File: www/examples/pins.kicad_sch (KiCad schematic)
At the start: 11 parts, among them U101 ATSAMD09C13A-SS, U102 ATSAMD09C13A-SS, U103 ATSAMD09C13A-SS, U104 ATSAMD09C13A-SS, U105 ATSAMD09C13A-SS, U106 ATSAMD09C13A-SS, U107 ATSAMD09C13A-SS, U108 ATSAMD09C13A-SS, U109 ATSAMD09C13A-SS, U110 ATSAMD09C13A-SS, U111 ATSAMD09C13A-SS

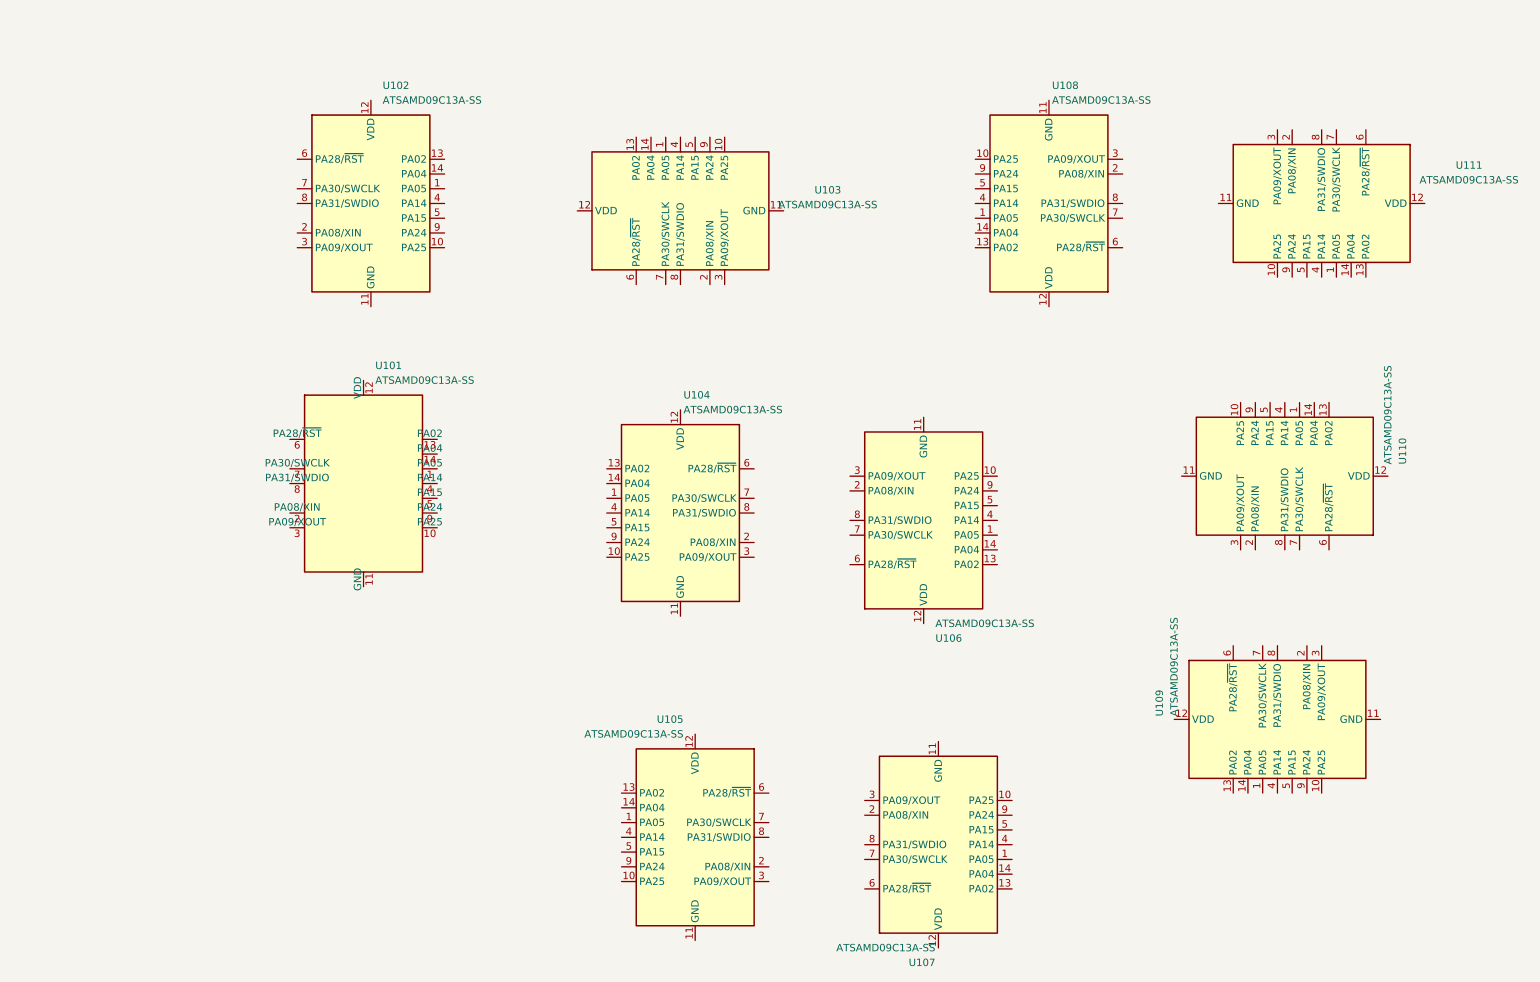
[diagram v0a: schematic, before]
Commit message: Add pins.kicad_sch to www/examples
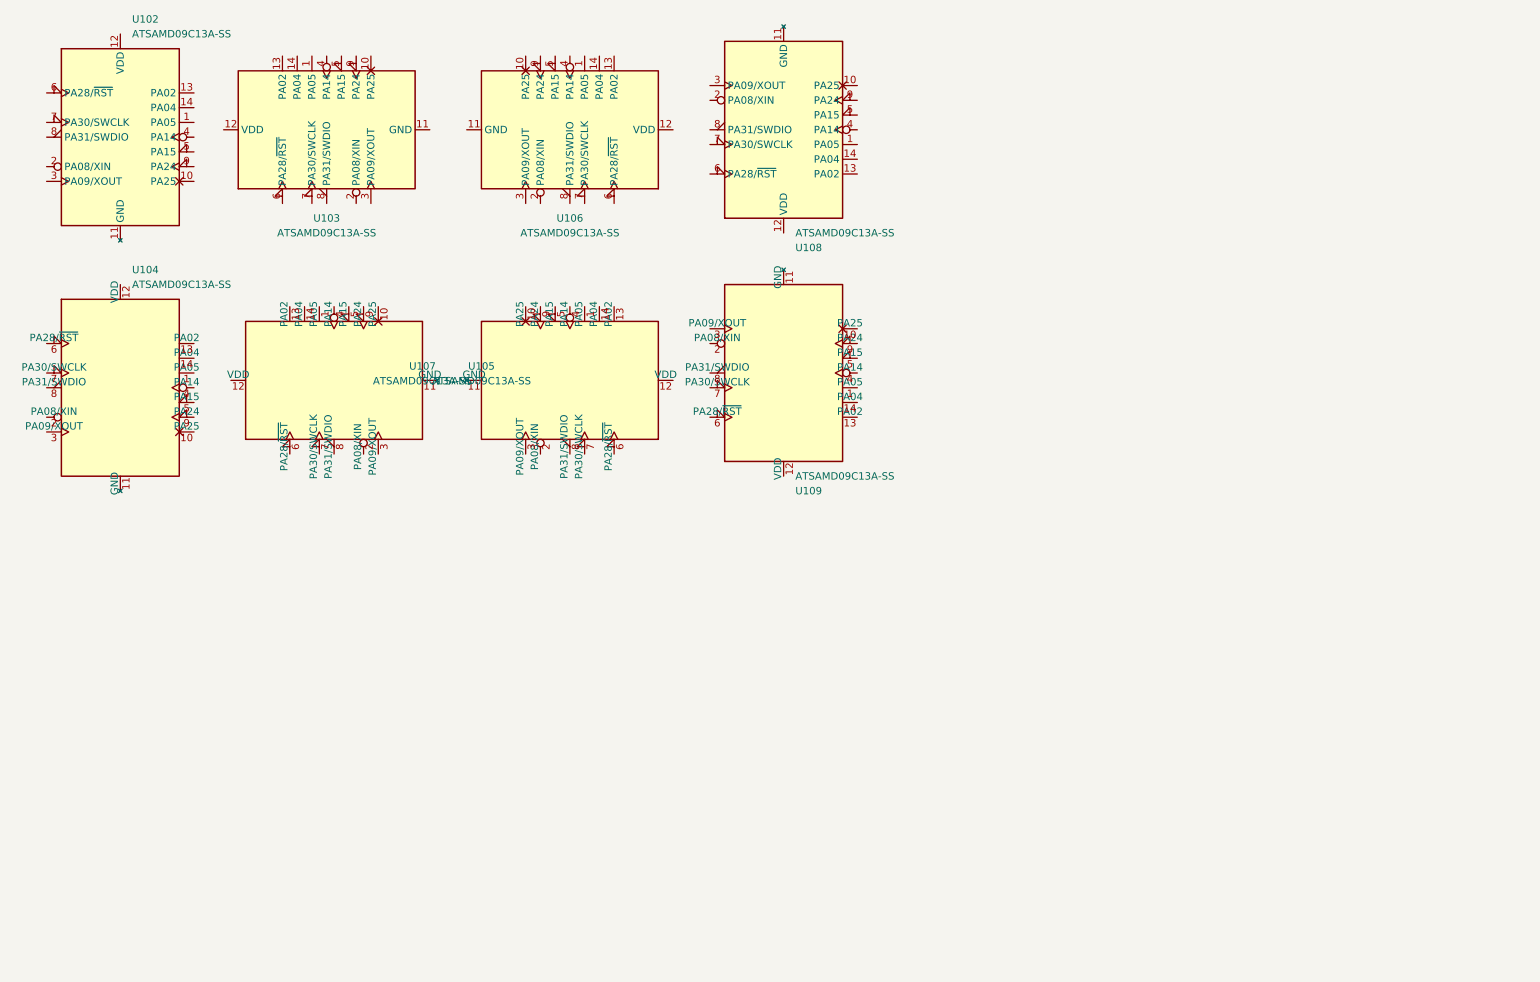
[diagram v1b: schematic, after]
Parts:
- removed U101, U110, U111: ATSAMD09C13A-SS, Package_SO:SOIC-14_3.9x8.7mm_P1.27mm, symbol MCU_Microchip_SAMD:ATSAMD09C13A-SS
